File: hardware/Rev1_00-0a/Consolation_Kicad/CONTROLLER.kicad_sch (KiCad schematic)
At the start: 65 parts, among them J11 5051102291, J13 5051102291, U2 RP2350A, U8 GD25Q32CWIGR, Y1 12MHz 10pF

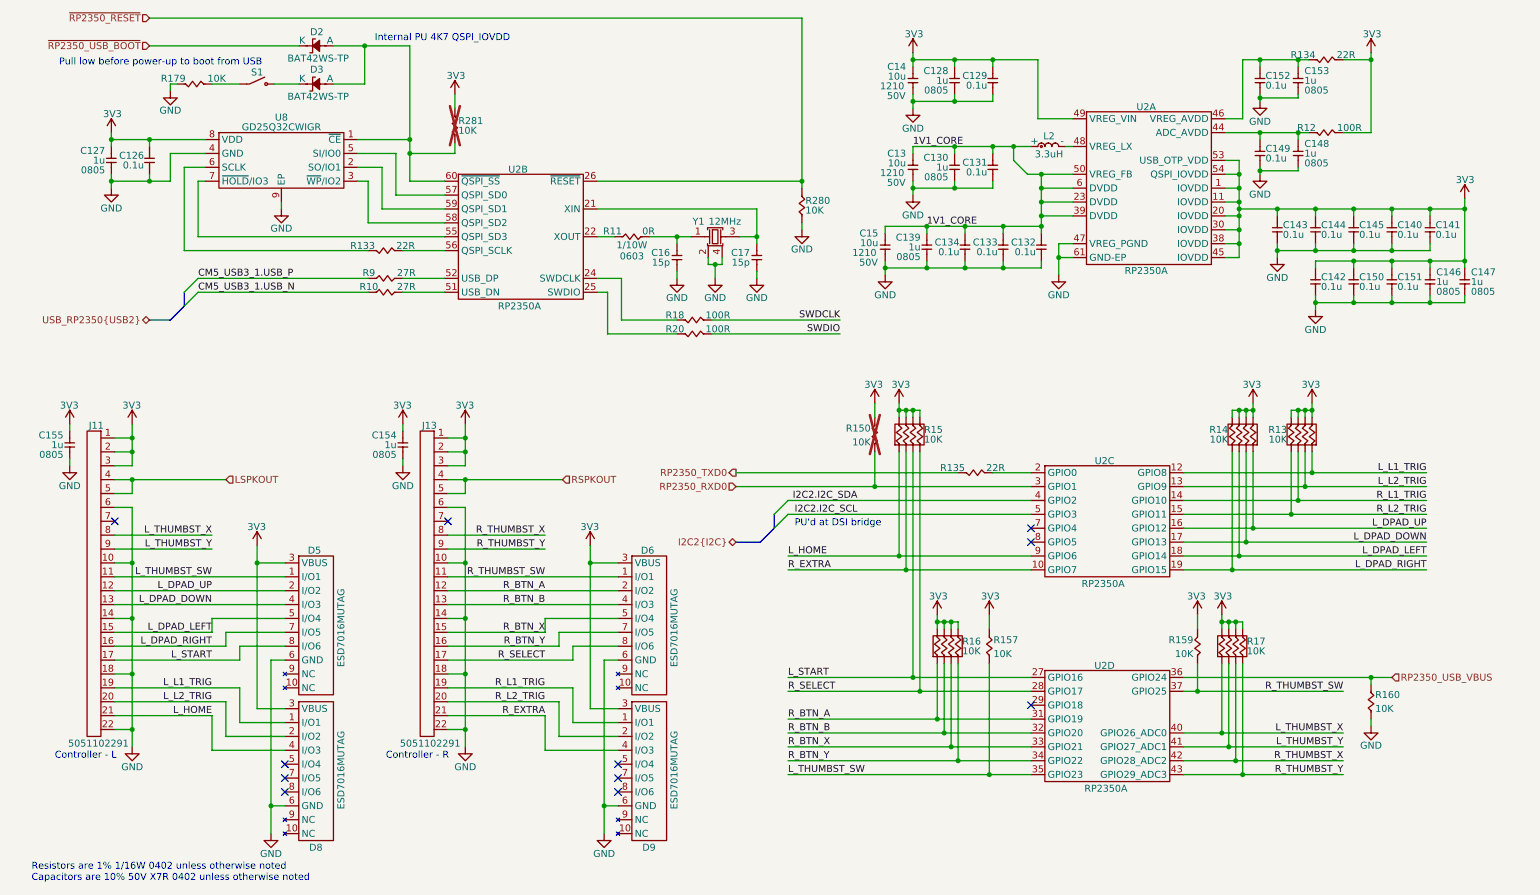
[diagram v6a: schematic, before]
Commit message: Major update to consolation schematics to include - Power supply - RESET SUPERVISOR - Review of GPIO and pinmux
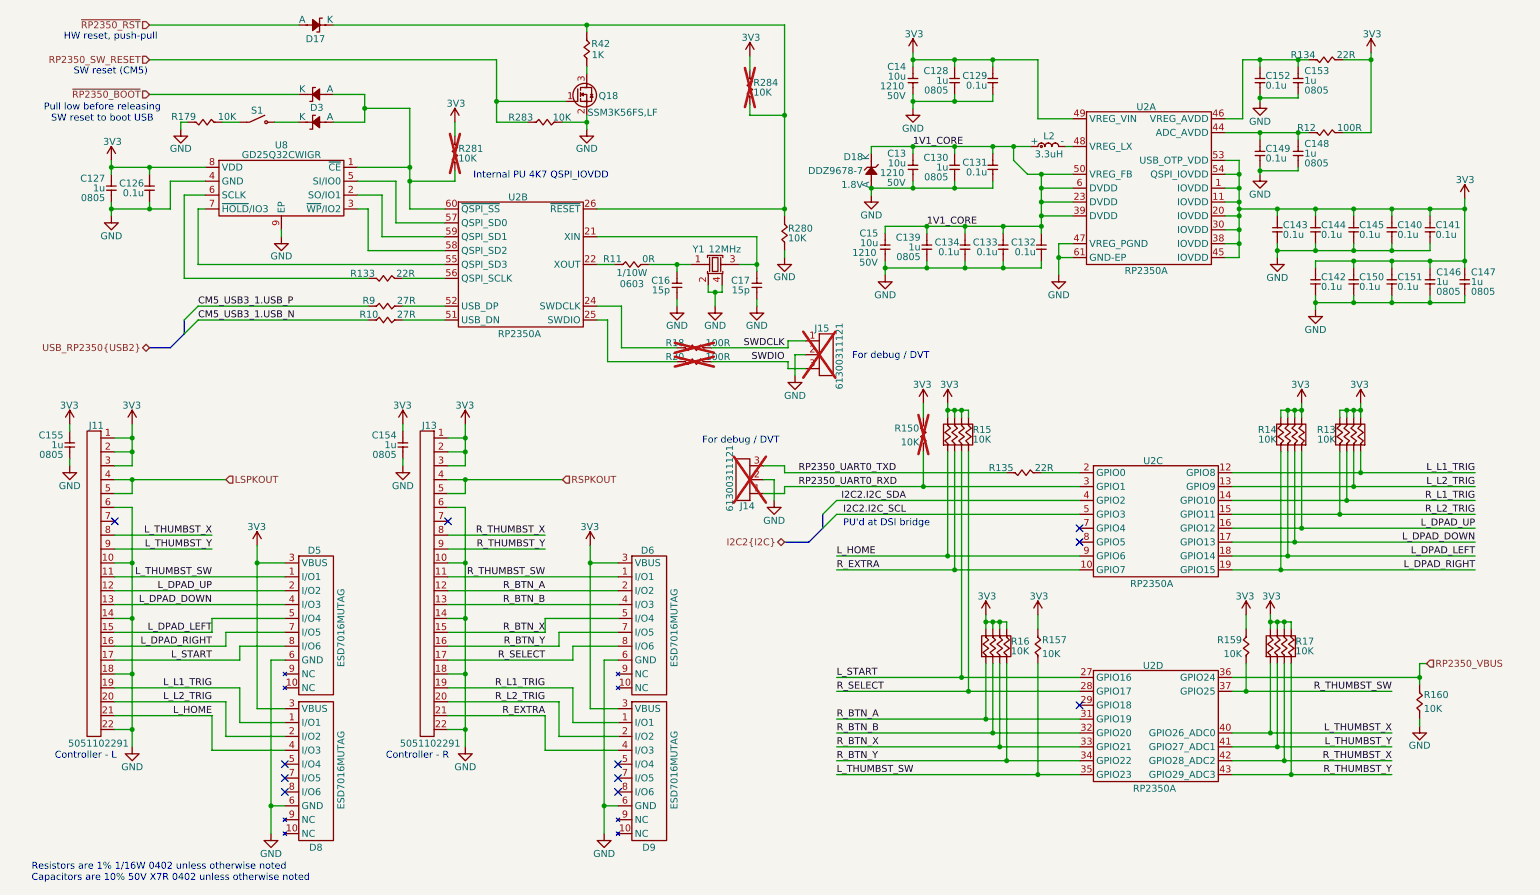
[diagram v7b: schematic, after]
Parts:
- added D17: BAT42WS-TP, footprint:SOD-323, symbol KicadCompDb:Diodes/DIODE_00006
- added D18: DDZ9678-7, footprint:SOD-123, symbol KicadCompDb:Diodes/DIODE_00002
- added J14, J15: 61300311121, footprint:HEADER_3P_2_54MM, symbol KicadCompDb:Connector/CONN_00001
- added Q18: SSM3K56FS,LF, footprint:SC-75, symbol KicadCompDb:Mosfet/MOSFET_00002
- added R283, R284: 10K, footprint:RES_0402, symbol KicadCompDb:Resistors/RES_SMT_00013
- added R42: 1K, footprint:RES_0402, symbol KicadCompDb:Resistors/RES_SMT_00004
- R18, R20: now not fitted
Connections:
- net 1V1_CORE: now also D18.1 (K)
- net 3V3: now also R284.2
- net GND: now also D18.2 (A), J14.2, J15.2, Q18.2 (S), R283.1
- net SWDCLK: now also J15.1
- net SWDIO: now also J15.3
- net RP2350_RXD0 renamed RP2350_UART0_RXD
- net RP2350_UART0_RXD: now also J14.1
- net RP2350_TXD0 renamed RP2350_UART0_TXD
- net RP2350_UART0_TXD: now also J14.3
- net RP2350_USB_VBUS renamed RP2350_VBUS
- net ~{RP2350_RESET}: no longer names the net of R280.2, U2.26 (~{RESET})
- net ~{RP2350_RESET}: now also D17.1 (K), R284.1, R42.2
- net ~{RP2350_USB_BOOT} renamed ~{RP2350_BOOT}
- new net: Q18.3 (D), R42.1
- new net RP2350_SW_RESET: Q18.1 (G), R283.2
- new net ~{RP2350_RST}: D17.2 (A)
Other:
- note added: "For debug / DVT"
- note added: "HW reset, push-pull"
- note added: "Pull low before releasing SW reset to boot USB"
- note added: "SW reset (CM5)"
- note removed: "Pull low before power-up to boot from USB"
- moved on the sheet: C126, C127, C16, C17, D3, R10, R11, R13, R133, R135, R14, R15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
